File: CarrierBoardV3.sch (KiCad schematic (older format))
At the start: 1 part

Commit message: Edited the schematic
Included the MSATA connector, have not finished it yet though.
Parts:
- added U?: MSATA-Socket, symbol CarrierBoardV3:MSATA-Socket
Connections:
- net mCOM_12V: now also J?.A1 (VDD_IN), J?.A2 (VDD_IN), J?.A50 (VDD_RTC_), J?.B1 (VDD_IN), J?.B2 (VDD_IN), J?.C1 (VDD_IN), J?.C2 (VDD_IN)
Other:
- note added: "TX2i Connector (SEAM-50-02.0-S-08-2-A-K-TR)"
- note removed: "Is either just VDD pins or something I do not know to connect too"
- moved on the sheet: J?

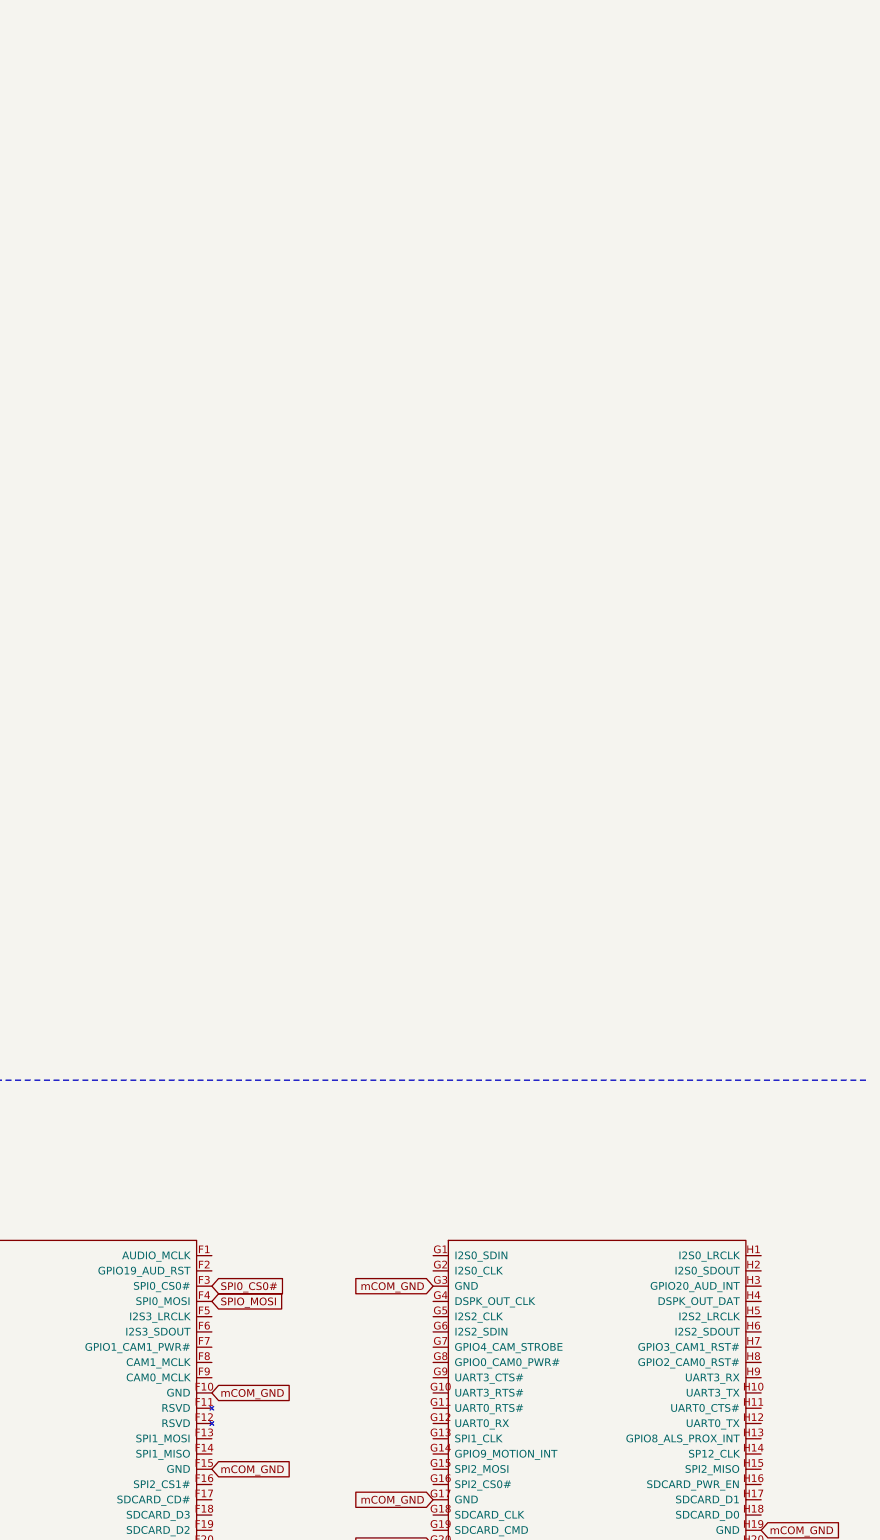
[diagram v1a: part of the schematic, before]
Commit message: Add PC104 connector
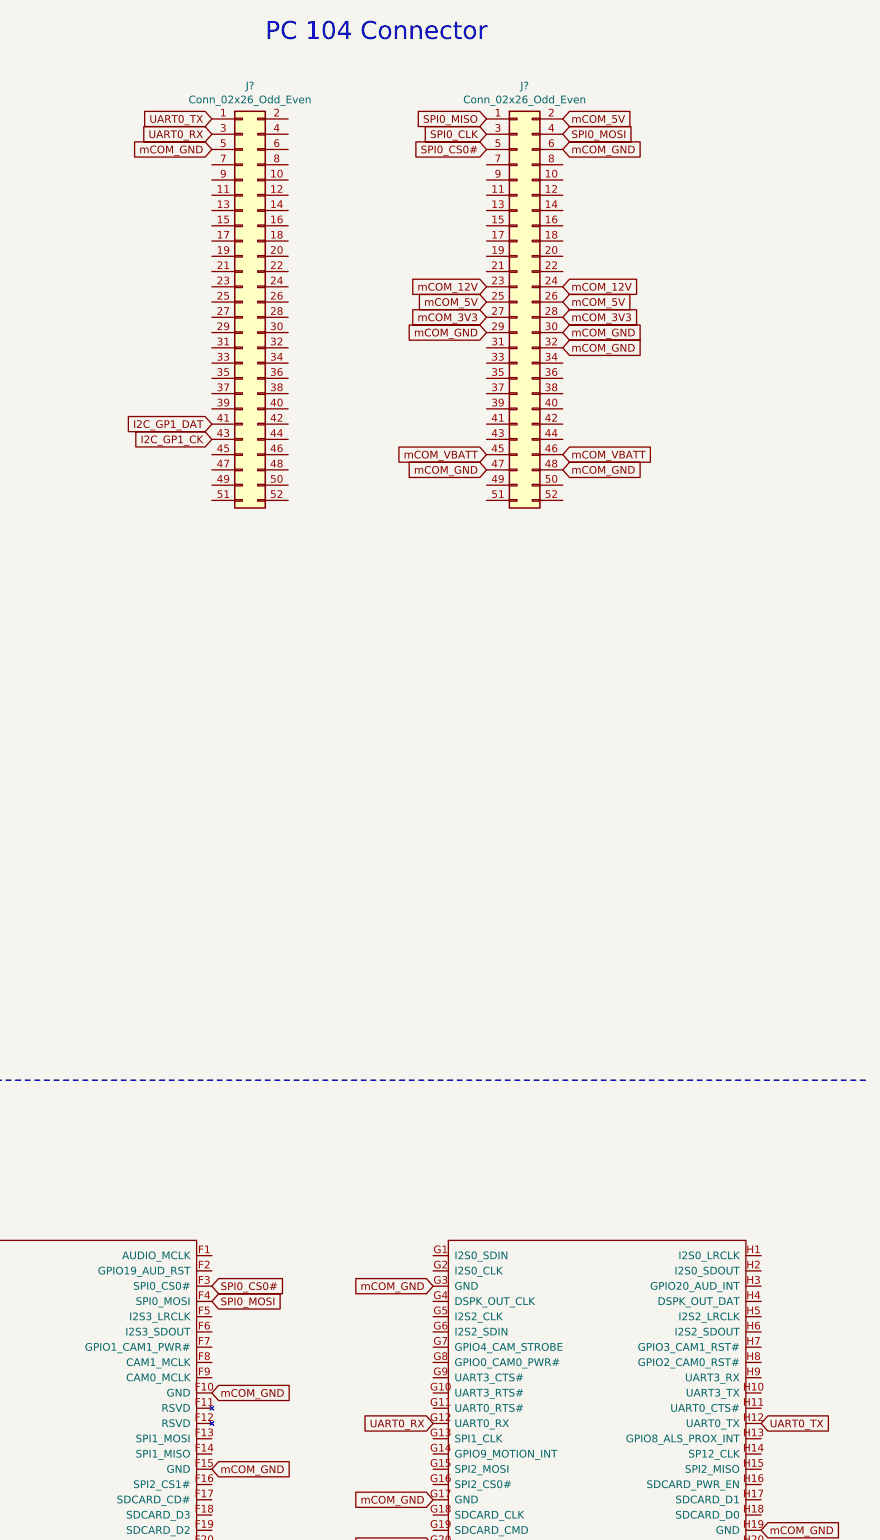
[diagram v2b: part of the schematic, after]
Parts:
- added J? (x2): Conn_02x26_Odd_Even, symbol Connector_Generic:Conn_02x26_Odd_Even
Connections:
- net I2C_GP1_CK: now also J?.43 (Pin_43)
- net I2C_GP1_DAT: now also J?.41 (Pin_41)
- net SPI0_CLK: now also J?.3 (Pin_3)
- net SPI0_CS0#: now also J?.5 (Pin_5)
- net SPI0_MISO: now also J?.1 (Pin_1)
- net mCOM_12V: now also J?.23 (Pin_23), J?.24 (Pin_24)
- net mCOM_GND: now also J?.29 (Pin_29), J?.30 (Pin_30), J?.32 (Pin_32), J?.47 (Pin_47), J?.48 (Pin_48), J?.5 (Pin_5), J?.6 (Pin_6)
- net UART0_RX: now reaches J?.G12 (UART0_RX)
- net UART0_RX: now also J?.3 (Pin_3)
- net UART0_TX: now reaches J?.H12 (UART0_TX)
- net UART0_TX: now also J?.1 (Pin_1)
- net SPIO_MOSI renamed SPI0_MOSI
- net SPI0_MOSI: now also J?.4 (Pin_4)
- new net mCOM_3V3: J?.27 (Pin_27), J?.28 (Pin_28)
- new net mCOM_5V: J?.2 (Pin_2), J?.25 (Pin_25), J?.26 (Pin_26)
- new net mCOM_VBATT: J?.45 (Pin_45), J?.46 (Pin_46)
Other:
- note added: "PC 104 Connector"
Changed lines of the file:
@@
 SPI0_CLK
 Text GLabel 18600 9700 2    50   Input ~ 0
-SPIO_MOSI
+SPI0_MOSI
 Text GLabel 18600 9600 2    50   Input ~ 0
 SPI0_CS0#
@@
 Wire Notes Line
 	8250 8250 22900 8250
+$Comp
+L Connector_Generic:Conn_02x26_Odd_Even J?
+U 1 1 5C65D725
+P 20600 3150
+F 0 "J?" H 20650 4567 50  0000 C CNN
+F 1 "Conn_02x26_Odd_Even" H 20650 4476 50  0000 C CNN
+F 2 "" H 20600 3150 50  0001 C CNN
+F 3 "~" H 20600 3150 50  0001 C CNN
+	1    20600 3150
+	1    0    0    -1
+$EndComp
+$Comp
+L Connector_Generic:Conn_02x26_Odd_Even J?
+U 1 1 5C65D93F
+P 18800 3150
+F 0 "J?" H 18850 4567 50  0000 C CNN
+F 1 "Conn_02x26_Odd_Even" H 18850 4476 50  0000 C CNN
+F 2 "" H 18800 3150 50  0001 C CNN
+F 3 "~" H 18800 3150 50  0001 C CNN
+	1    18800 3150
+	1    0    0    -1
+$EndComp
+Text GLabel 20400 3050 0    50   Input ~ 0
+mCOM_12V
+Text GLabel 20900 3050 2    50   Input ~ 0
+mCOM_12V
+Text GLabel 20900 3150 2    50   Input ~ 0
+mCOM_5V
+Text GLabel 20400 3150 0    50   Input ~ 0
+mCOM_5V
+Text GLabel 20400 3250 0    50   Input ~ 0
+mCOM_3V3
+Text GLabel 20900 3250 2    50   Input ~ 0
+mCOM_3V3
+Text GLabel 20900 3350 2    50   Input ~ 0
+mCOM_GND
+Text GLabel 20900 3450 2    50   Input ~ 0
+mCOM_GND
+Text GLabel 20400 3350 0    50   Input ~ 0
+mCOM_GND
+Text GLabel 20400 4250 0    50   Input ~ 0
+mCOM_GND
+Text GLabel 20900 4250 2    50   Input ~ 0
+mCOM_GND
+Text GLabel 20900 4150 2    50   Input ~ 0
+mCOM_VBATT
+Text GLabel 20400 4150 0    50   Input ~ 0
+mCOM_VBATT
+Text GLabel 18600 3950 0    50   Input ~ 0
+I2C_GP1_DAT
+Text GLabel 18600 4050 0    50   Input ~ 0
+I2C_GP1_CK
+Text GLabel 20050 10500 0    50   Input ~ 0
+UART0_RX
+Text GLabel 22200 10500 2    50   Input ~ 0
+UART0_TX
+Text GLabel 18600 1950 0    50   Input ~ 0
+UART0_TX
+Text GLabel 18600 2050 0    50   Input ~ 0
+UART0_RX
+Text GLabel 18600 2150 0    50   Input ~ 0
+mCOM_GND
+Text GLabel 20400 2150 0    50   Input ~ 0
+SPI0_CS0#
+Text GLabel 20400 2050 0    50   Input ~ 0
+SPI0_CLK
+Text GLabel 20400 1950 0    50   Input ~ 0
+SPI0_MISO
+Text GLabel 20900 2050 2    50   Input ~ 0
+SPI0_MOSI
+Text GLabel 20900 2150 2    50   Input ~ 0
+mCOM_GND
+Text GLabel 20900 1950 2    50   Input ~ 0
+mCOM_5V
+Text Notes 18950 1450 0    118  ~ 0
+PC 104 Connector
 $EndSCHEMATC

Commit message: Schematic Update Minus Ethernet & USB to RS232
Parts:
- added C27, C28, C29: .1uF, symbol Device:CP
- added C7, C?: 47nF, symbol Device:C
- added C8: 33uF, symbol Device:C
- added D5: D_Zener, symbol Device:D_Zener
- added D6, D7, D8: LED, symbol Device:LED
- added J10: Conn_02x03_Odd_Even, symbol Connector_Generic:Conn_02x03_Odd_Even
- added J6: Conn_01x03_Male, symbol Connector_Generic:Conn_01x03
- added J7: Conn_01x03_Male, symbol Connector:Conn_01x03_Male
- added J8: Conn_01x06_Male, symbol Connector:Conn_01x06_Male
- added J9: Conn_02x04_Odd_Even, symbol Connector_Generic:Conn_02x04_Odd_Even
- added J?: USB_B_Mini, symbol CarrierBoardV3:USB_B_Mini
- added R11, R12, R13: 10k, symbol Device:R
- added R23: 330, symbol Device:R
- added R24: 180, symbol Device:R
- added R25: 1k, symbol Device:R
- added R32: 0, symbol Device:R
- added SW1, SW2, SW3: SW_Push, symbol Switch:SW_Push
- added U?: FT232RQ, symbol CarrierBoardV3:FT232RQ
- gave numbers to parts that had none: 1
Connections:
- net labels added: +3.3V, GNDREF, I2C_CK, I2C_DAT, SPI0_CS#, SPI0_POWER, TX2i_12V, TX2i_3V3, TX2i_5V, TX2i_5V_SBY, TX2i_GND, TX2i_RX, TX2i_TX, TX2i_VBATT
- net labels removed: mCOM_12V, mCOM_3V3, mCOM_5V, mCOM_GND, mCOM_VBATT
- wire segments 0 -> 59
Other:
- note added: "12V"
- note added: "3V3"
- note added: "5V SBY"
- note added: "Break Out"
- note added: "GPIO"
- note added: "I2C"
- note added: "LED Indicators"
- note added: "MISC SHIT"
- note added: "Rs232"
- note added: "SATA Connector"
- note added: "SPI"
- note added: "TEST/Power Buttons"
- moved on the sheet: J?, U9

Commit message: Edited Schematic
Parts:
- removed J?: USB_B_Mini, symbol CarrierBoardV3:USB_B_Mini
- added C10, C6: .1uF, symbol Device:C
- added C11, C12: .33uF, symbol Device:CP
- added C9: 4.7uF, symbol Device:C
- added D1: Power_Protection:SP0502BAJT, Package_TO_SOT_SMD:SOT-323_SC-70, symbol CarrierBoardV3:Power_Protection_SP0502BAJT
- added D2, D3: LED, symbol Device:LED
- added J4: Conn_02x09_Odd_Even, symbol Connector_Generic:Conn_02x09_Odd_Even
- added J?: USB_B_Mini, symbol CarrierBoardV3:USB_B_Mini
- added R10, R14: 10K, symbol Device:R
- added R15: 4.7K, symbol Device:R
- added R16, R9: 330, symbol Device:R
- added R17, R18: 200, symbol Device:R
- added U?: Interface_UART:MAX3221, symbol CarrierBoardV3:Interface_UART_MAX3221
- C8: value 33uF -> .33uF
- U9: footprint (none) -> CarrierBoardV3:MSATA-Socket
- gave numbers to parts that had none: 1
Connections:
- net labels added: GBE_CTREF(GND), RXD, Reset#, TXD
- wire segments 59 -> 156
- no-connect marks 0 -> 17
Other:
- note added: "Ethernet"
- note added: "USB to RS232"
- moved on the sheet: C7, C8, C?, U4

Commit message: Assigned all footprints except TX2i connector
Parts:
- removed D1: Power_Protection:SP0502BAJT, Package_TO_SOT_SMD:SOT-323_SC-70, symbol CarrierBoardV3:Power_Protection_SP0502BAJT
- removed R32: 0, symbol Device:R
- removed U?: Interface_UART:MAX3221, symbol CarrierBoardV3:Interface_UART_MAX3221
- added D1: SP0502BAJT, Package_TO_SOT_SMD:SOT-323_SC-70, symbol Power_Protection:SP0502BAJT
- added TP?: TestPoint, TestPoint:TestPoint_Pad_4.0x4.0mm, symbol Connector:TestPoint
- added U3: MAX3221, Package_SO:TSSOP-16_4.4x5mm_P0.65mm, symbol Interface_UART:MAX3221
- C10, C6, C7, C8, C9: footprint (none) -> Capacitor_SMD:C_0603_1608Metric
- C11, C12, C27, C28, C29: footprint (none) -> Capacitor_SMD:CP_Elec_4x4.5
- C6: renamed from C?; footprint (none) -> Capacitor_SMD:C_0603_1608Metric
- D2, D3, D5, D6, D7, D8: footprint (none) -> LED_SMD:LED_0603_1608Metric
- J10: footprint (none) -> Connector_PinHeader_2.54mm:PinHeader_2x03_P2.54mm_Vertical
- J4: footprint (none) -> CarrierBoardV3:Ethernet
- J5: renamed from J?; footprint (none) -> Connectors_USB:USB_Micro-B_Molex-105017-0001
- J6: footprint (none) -> Connector_PinHeader_1.00mm:PinHeader_1x03_P1.00mm_Vertical
- J7: footprint (none) -> Connector_PinHeader_2.54mm:PinHeader_1x03_P2.54mm_Vertical
- J8: footprint (none) -> Connector_PinHeader_2.54mm:PinHeader_1x06_P2.54mm_Vertical
- J9: footprint (none) -> Connector_PinHeader_2.54mm:PinHeader_2x04_P2.54mm_Vertical
- R10, R11, R12, R13, R14, R15, R16, R17, R18, R23, R24, R25, R9: footprint (none) -> Resistor_SMD:R_0603_1608Metric
- SW1, SW2, SW3: footprint (none) -> Button_Switch_SMD:SW_SPST_B3S-1000
- U4: footprint (none) -> Package_DFN_QFN:QFN-32-1EP_5x5mm_P0.5mm_EP3.1x3.1mm
- gave numbers to parts that had none: 3
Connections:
- wire segments 156 -> 157

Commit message: Fixed errors in schematic numbering
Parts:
- D1: symbol Power_Protection:SP0502BAJT -> CarrierBoardV3-rescue:SP0502BAJT-Power_Protection
- gave numbers to parts that had none: 1
- renumbered C6 to C1, C12 to C10, C29 to C11, C6 to C2, C7 to C3, C8 to C4, C9 to C5, C27 to C6, C28 to C7, C10 to C8, C11 to C9, D5 to D4, D7 to D5, D8 to D7, J8 to J10, J5 to J4, J4 to J5, J9 to J6, J6 to J7, J10 to J8, J7 to J9, R10 to R1, R16 to R10, R14 to R2, R15 to R3, R17 to R4, R18 to R5, R23 to R6, R24 to R7, R25 to R8, U3 to U1, U4 to U2, U9 to U3

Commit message: Added footprints for TX2i connector and PC-104 connector
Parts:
- J1: footprint (none) -> CarrierBoardV3:SEAM-50-02.0-XX-08-X-A
- J2, J3: footprint (none) -> Connector_PinHeader_1.00mm:PinHeader_2x26_P1.00mm_Vertical
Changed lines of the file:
@@
 F 0 "J1" H 15700 14265 50  0000 C CNN
 F 1 "TX2iConnctor" H 15700 14174 50  0000 C CNN
-F 2 "" H 18350 12200 50  0001 C CNN
+F 2 "CarrierBoardV3:SEAM-50-02.0-XX-08-X-A" H 18350 12200 50  0001 C CNN
 F 3 "" H 18350 12200 50  0001 C CNN
 	1    15550 11700
@@
 F 0 "J3" H 20900 7767 50  0000 C CNN
 F 1 "Conn_02x26_Odd_Even" H 20900 7676 50  0000 C CNN
-F 2 "" H 20850 6350 50  0001 C CNN
+F 2 "Connector_PinHeader_1.00mm:PinHeader_2x26_P1.00mm_Vertical" H 20850 6350 50  0001 C CNN
 F 3 "~" H 20850 6350 50  0001 C CNN
 	1    20850 6350
@@
 F 0 "J2" H 19500 7767 50  0000 C CNN
 F 1 "Conn_02x26_Odd_Even" H 19500 7676 50  0000 C CNN
-F 2 "" H 19450 6350 50  0001 C CNN
+F 2 "Connector_PinHeader_1.00mm:PinHeader_2x26_P1.00mm_Vertical" H 19450 6350 50  0001 C CNN
 F 3 "~" H 19450 6350 50  0001 C CNN
 	1    19450 6350

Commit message: Fixed PC104 footprint
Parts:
- J2, J3: footprint Connector_PinHeader_1.00mm:PinHeader_2x26_P1.00mm_Vertical -> CarrierBoardV3:ESQ-126-XX-X-D
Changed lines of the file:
@@
 F 0 "J3" H 20900 7767 50  0000 C CNN
 F 1 "Conn_02x26_Odd_Even" H 20900 7676 50  0000 C CNN
-F 2 "Connector_PinHeader_1.00mm:PinHeader_2x26_P1.00mm_Vertical" H 20850 6350 50  0001 C CNN
+F 2 "CarrierBoardV3:ESQ-126-XX-X-D" H 20850 6350 50  0001 C CNN
 F 3 "~" H 20850 6350 50  0001 C CNN
 	1    20850 6350
@@
 F 0 "J2" H 19500 7767 50  0000 C CNN
 F 1 "Conn_02x26_Odd_Even" H 19500 7676 50  0000 C CNN
-F 2 "Connector_PinHeader_1.00mm:PinHeader_2x26_P1.00mm_Vertical" H 19450 6350 50  0001 C CNN
+F 2 "CarrierBoardV3:ESQ-126-XX-X-D" H 19450 6350 50  0001 C CNN
 F 3 "~" H 19450 6350 50  0001 C CNN
 	1    19450 6350
